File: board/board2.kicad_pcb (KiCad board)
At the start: 2 copper layers, 88 x 64 mm, 72 parts, among them J1 Battery, J2 Conn_01x06_Male, J3 Conn_ARM_JTAG_SWD_10, J4 Range_Front, J5 Range_Left, J6 Range_Right, J7 Battery, J8 Conn_02x06_Odd_Even, SW1 RST, SW2 SW_Push, SW3 SW_Push, SW4 SW_Push, U1 MIC5205-3.3YM5, U2 STM32F405RGTx, U3 DRV8848, U4 Left_Motor, U5 Right_Motor, Y1 DNP

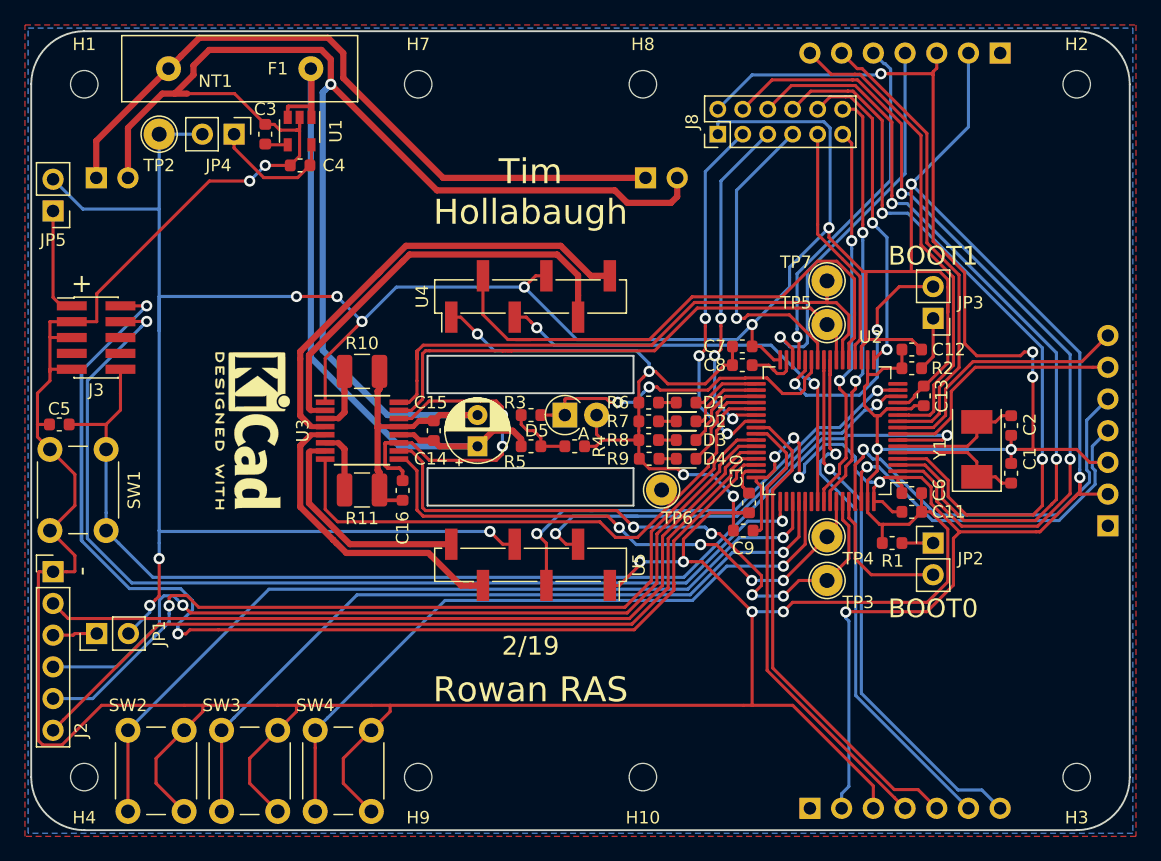
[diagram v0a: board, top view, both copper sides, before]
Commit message: Board redesign
 - add IMU6500
 - only one battery
 - half the size
 - op amp buffer on battery monitor
 - 4 layer board
 - and more
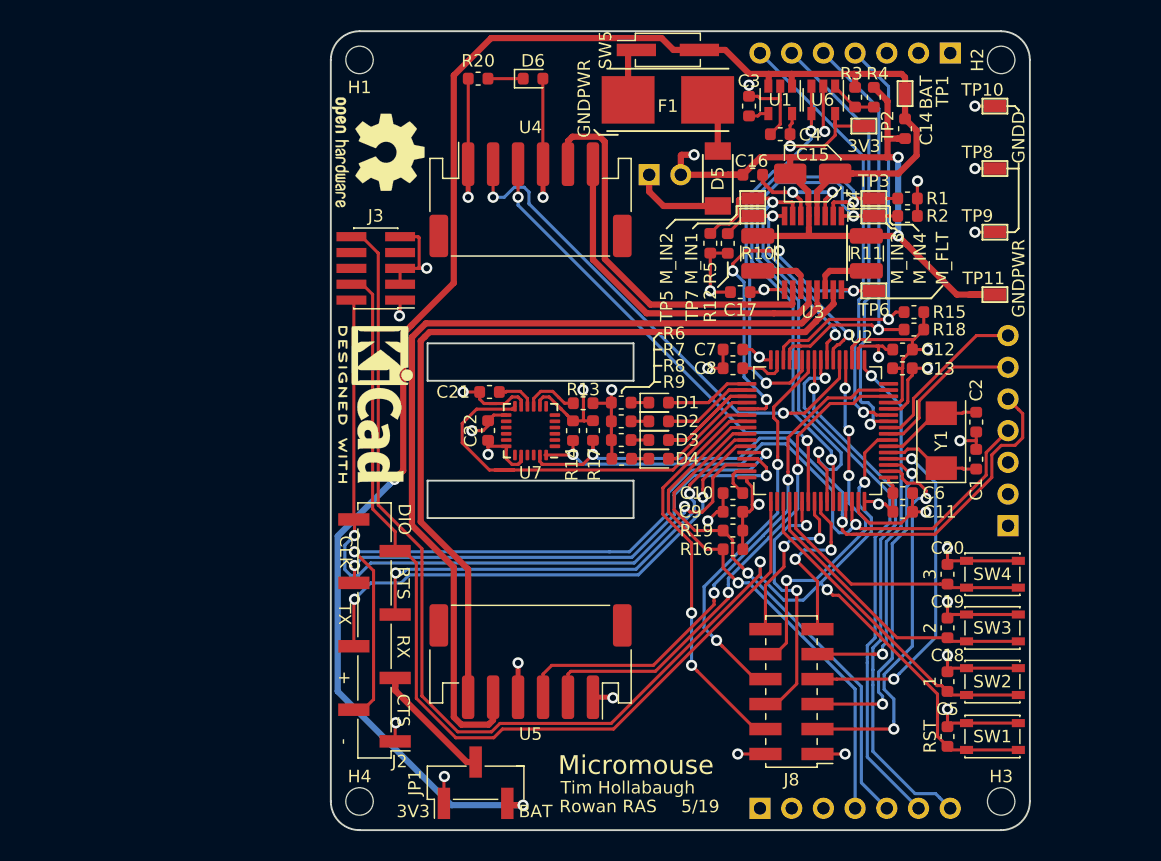
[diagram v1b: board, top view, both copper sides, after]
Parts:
- removed H10, H7, H8, H9: MountingHole, MountingHole:MountingHole_2.2mm_M2
- removed J7: Battery, Connector_PinHeader_2.54mm:PinHeader_1x02_P2.54mm_Horizontal
- removed JP2: BOOT0, Connector_PinHeader_2.54mm:PinHeader_1x02_P2.54mm_Vertical
- removed JP3: BOOT1, Connector_PinHeader_2.54mm:PinHeader_1x02_P2.54mm_Vertical
- removed JP4: BAT_PWR, Connector_PinHeader_2.54mm:PinHeader_1x02_P2.54mm_Vertical
- removed JP5: PROG_PWR, Connector_PinHeader_2.54mm:PinHeader_1x02_P2.54mm_Vertical
- added C17: 0.1uF, Capacitor_SMD:C_0603_1608Metric, F.Cu at (116.8, 88.9)
- added C18: 0.1uF, Capacitor_SMD:C_0603_1608Metric, F.Cu at (133.4, 120.1)
- added C19: 0.1uF, Capacitor_SMD:C_0603_1608Metric, F.Cu at (133.4, 115.8)
- added C20: 0.1uF, Capacitor_SMD:C_0603_1608Metric, F.Cu at (133.4, 111.5)
- added C21: 0.1uF, Capacitor_SMD:C_0603_1608Metric, F.Cu at (96.7, 96.9)
- added C22: 0.1uF, Capacitor_SMD:C_0603_1608Metric, F.Cu at (96.6, 100.0)
- added D6: WHITE, LED_SMD:LED_0603_1608Metric, F.Cu at (100.2, 71.8)
- added R12: 10k, Resistor_SMD:R_0603_1608Metric, F.Cu at (115.8, 85.0)
- added R13: 10k, Resistor_SMD:R_0603_1608Metric, F.Cu at (104.2, 97.8)
- added R14: 2.2K, Resistor_SMD:R_0603_1608Metric, F.Cu at (103.4, 100.0)
- added R15: 2.2K, Resistor_SMD:R_0603_1608Metric, F.Cu at (130.7, 90.5)
- added R16: 2.2K, Resistor_SMD:R_0603_1608Metric, F.Cu at (116.2, 109.5)
- added R17: 2.2K, Resistor_SMD:R_0603_1608Metric, F.Cu at (105.0, 100.0)
- added R18: 2.2K, Resistor_SMD:R_0603_1608Metric, F.Cu at (130.7, 91.9)
- added R19: 2.2K, Resistor_SMD:R_0603_1608Metric, F.Cu at (116.2, 108.0)
- added R20: 330, Resistor_SMD:R_0603_1608Metric, F.Cu at (95.8, 71.8)
- added REF**: OSHW-Logo2_9.8x8mm_SilkScreen, Symbol:OSHW-Logo2_9.8x8mm_SilkScreen, F.Cu at (87.8, 77.7)
- added SW5: Power, Connector_PinHeader_2.54mm:PinHeader_2x01_P2.54mm_Vertical_SMD, F.Cu at (111.0, 69.5)
- added TP1: BAT, micromouse_custom:TestPoint_Pad_1.8x1.0mm, F.Cu at (130.0, 73.0)
- added TP10: GND, micromouse_custom:TestPoint_Pad_1.8x1.0mm, F.Cu at (137.2, 74.0)
- added TP11: GND, micromouse_custom:TestPoint_Pad_1.8x1.0mm, F.Cu at (137.2, 89.1)
- added TP8: GND, micromouse_custom:TestPoint_Pad_1.8x1.0mm, F.Cu at (137.2, 79.0)
- added TP9: GND, micromouse_custom:TestPoint_Pad_1.8x1.0mm, F.Cu at (137.2, 84.1)
- added U6: MCP6001U, Package_TO_SOT_SMD:SOT-23-5, F.Cu at (123.5, 73.5)
- added U7: MPU-6500, Sensor_Motion:InvenSense_QFN-24_4x4mm_P0.5mm, F.Cu at (100.0, 100.0)
- C15: footprint Capacitor_THT:CP_Radial_D5.0mm_P2.50mm -> Capacitor_SMD:CP_Elec_4x4.5
- D1: value LED -> RED
- D2: value LED -> GREEN
- D3: value LED -> BLUE
- D4: value LED -> ORANGE
- D5: value D_Zener -> DB2441700L; footprint Diode_THT:D_T-1_P2.54mm_Vertical_AnodeUp -> micromouse_custom:SC-110A-2
- F1: value 2A -> 1A; footprint Fuse:Fuse_Littelfuse-LVR100 -> micromouse_custom:Littlefuse_154
- H1, H2, H3, H4: value MountingHole -> Corner
- J2: value Conn_01x06_Male -> Serial; footprint Connector_PinHeader_2.54mm:PinHeader_1x06_P2.54mm_Vertical -> Connector_PinHeader_2.54mm:PinHeader_1x08_P2.54mm_Vertical_SMD_Pin1Left
- J3: value Conn_ARM_JTAG_SWD_10 -> SWD
- J8: value Conn_02x06_Odd_Even -> Exp; footprint Connector_PinHeader_2.00mm:PinHeader_2x06_P2.00mm_Vertical -> Connector_PinHeader_2.00mm:PinHeader_2x06_P2.00mm_Vertical_SMD
- JP1: footprint Connector_PinHeader_2.54mm:PinHeader_1x02_P2.54mm_Vertical -> Connector_PinHeader_2.54mm:PinHeader_1x03_P2.54mm_Vertical_SMD_Pin1Left
- NT1: value Net-Tie_2 -> GND-Tie
- R1, R2: value 10K -> 10k
- R3: value 2k -> 200k
- R4: value 1k -> 100k
- R5: value 1k -> 10k
- SW1: footprint Button_Switch_THT:SW_PUSH_6mm -> Button_Switch_SMD:SW_SPST_PTS810
- SW2: value SW_Push -> Left; footprint Button_Switch_THT:SW_PUSH_6mm -> Button_Switch_SMD:SW_SPST_PTS810
- SW3: value SW_Push -> Right; footprint Button_Switch_THT:SW_PUSH_6mm -> Button_Switch_SMD:SW_SPST_PTS810
- SW4: value SW_Push -> Center; footprint Button_Switch_THT:SW_PUSH_6mm -> Button_Switch_SMD:SW_SPST_PTS810
- TP2, TP3, TP4, TP5, TP6, TP7: footprint TestPoint:TestPoint_THTPad_D2.5mm_Drill1.2mm -> micromouse_custom:TestPoint_Pad_1.8x1.0mm
- U4: footprint Connector_PinHeader_2.54mm:PinHeader_1x06_P2.54mm_Vertical_SMD_Pin1Left -> Connector_JST:JST_PH_S6B-PH-SM4-TB_1x06-1MP_P2.00mm_Horizontal
- U5: footprint Connector_PinHeader_2.54mm:PinHeader_1x06_P2.54mm_Vertical_SMD_Pin1Right -> Connector_JST:JST_PH_S6B-PH-SM4-TB_1x06-1MP_P2.00mm_Horizontal
- moved SW1 77.3 mm to (137.0, 124.5), turned to 0 degrees
- moved C5 75.4 mm to (133.4, 124.5), turned to 90 degrees
- moved SW2 70.0 mm to (137.0, 120.1), turned to 180 degrees
- moved SW3 63.5 mm to (137.0, 115.8), turned to 180 degrees
- moved SW4 57.5 mm to (137.0, 111.5), turned to 180 degrees
- moved TP2 56.5 mm to (126.7, 75.6)
- moved J8 45.0 mm to (120.9, 120.9), turned to 180 degrees
- moved C14 44.8 mm to (130.0, 75.8), turned to 270 degrees
- moved R11 44.6 mm to (126.9, 85.8), turned to 270 degrees
- moved J1 44.3 mm to (109.5, 79.5)
- moved NT1 40.9 mm to (112.6, 77.9)
- moved U3 38.8 mm to (122.6, 85.8), turned to 90 degrees
- moved C3 38.8 mm to (117.5, 74.0)
- moved U1 38.6 mm to (120.0, 73.5)
- moved C4 38.5 mm to (120.0, 76.2)
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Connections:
- C4 pad 1: Net-(C4-Pad1) -> +3V3
- D5 pad 1: /VBAT -> Net-(D5-Pad1)
- D5 pad 2: GNDD -> Net-(D5-Pad2)
- F1 pad 1: +BATT -> Net-(F1-Pad1)
- F1 pad 2: /BAT_IN -> Net-(D5-Pad1)
- J1 pad 1: /BAT_IN -> Net-(D5-Pad2)
- J3 pad 1: Net-(J3-Pad1) -> +3V3
- J3 pad 6: Net-(J3-Pad6) -> (no net)
- J3 pad 7: Net-(J3-Pad7) -> (no net)
- J3 pad 8: Net-(J3-Pad8) -> (no net)
- J4 pad 1: Net-(J4-Pad1) -> (no net)
- J5 pad 1: Net-(J5-Pad1) -> (no net)
- J6 pad 1: Net-(J6-Pad1) -> (no net)
- J6 pad 4: /R_SCL -> /R_SDA
- J6 pad 5: /R_SDA -> /R_SCL
- J8 pad 1: +3V3 -> GNDD
- J8 pad 10: /PA3 -> /PA4
- J8 pad 11: /PB4 -> /PB5
- J8 pad 12: /PB5 -> /PB4
- J8 pad 2: GNDD -> +3V3
- J8 pad 3: /PC8 -> /PC13
- J8 pad 4: /PC13 -> /PC8
- J8 pad 5: /PC7 -> /PC14
- J8 pad 6: /PC14 -> /PD2
- J8 pad 7: /PB0 -> /PC15
- J8 pad 8: /PC15 -> /PB0
- J8 pad 9: /PA4 -> /PA3
- JP1 pad 1: Net-(J2-Pad3) -> +3V3
- JP1 pad 2: +3V3 -> Net-(J2-Pad3)
- R1 pad 1: Net-(JP2-Pad1) -> /M_IN4
- R2 pad 1: Net-(JP3-Pad1) -> /M_IN3
- R4 pad 2: GNDD -> GNDPWR
- R5 pad 1: /VBAT -> /M_IN2
- R5 pad 2: Net-(R3-Pad2) -> GNDD
- U1 pad 5: Net-(C4-Pad1) -> +3V3
- U2 pad 16: /PA2 -> (no net)
- U2 pad 28: /BOOT1 -> (no net)
- U2 pad 38: /PC7 -> /IMU_INT
- U2 pad 50: /PA15 -> (no net)
- U2 pad 60: /BOOT0 -> (no net)
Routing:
- net GNDD: track 406.7 -> 125.3 mm, vias 15 -> 26
- net +3V3: track 355.3 -> 78.5 mm, vias 16 -> 13
- net +BATT: track 58.5 -> 132.7 mm, vias 0 -> 2
- net /BAT_IN: track 56.2 -> 0.00 mm
- net GNDPWR: track 116.0 -> 64.5 mm, vias 1 -> 2
- net /RM_2: track 24.5 -> 72.1 mm
- net /RM_1: track 18.2 -> 65.6 mm
- net /SWDIO: track 105.6 -> 60.0 mm
- net /BTN1: track 68.6 -> 26.7 mm, vias 1 -> 0
- net /BTN2: track 62.0 -> 24.3 mm, vias 1 -> 0
- net /PC14: track 64.4 -> 27.1 mm
- net /PC13: track 68.2 -> 31.2 mm
- net /IMU_INT: track 0.00 -> 34.0 mm
- net /BTN3: track 55.3 -> 21.5 mm, vias 1 -> 0
- net /PC15: track 60.6 -> 27.8 mm
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- added copper zone on In2.Cu, net +3V3
- added copper zone on In1.Cu, net GNDD
- removed copper zone on B.Cu, net +3V3
- removed copper zone on F.Cu, net GNDD
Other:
- board size 88 x 64 mm -> 56 x 64 mm
- copper layers 2 -> 4
- board text added: "1"
- board text added: "2"
- board text added: "3"
- board text added: "3V3"
- board text added: "5/19"
- board text added: "BAT"
- board text added: "CLK"
- board text added: "CTS"
- board text added: "DIO"
- board text added: "GNDD"
- board text added: "GNDPWR"
- board text added: "M_FLT"
- board text added: "M_IN1"
- board text added: "M_IN2"
- board text added: "M_IN3"
- board text added: "M_IN4"
- board text added: "Micromouse"
- board text added: "RST"
- board text added: "RTS"
- board text added: "RX"
- board text added: "TX"
- board text added: "Tim Hollabaugh"
- board text removed: "2/19"
- board text removed: "BOOT0"
- board text removed: "BOOT1"
- board text removed: "Battery 2"
- board text removed: "Hollabaugh"
- board text removed: "Tim"

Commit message: Final board layout
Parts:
- removed JP1: UART_PWR, Connector_PinHeader_2.54mm:PinHeader_1x03_P2.54mm_Vertical_SMD_Pin1Left
- added J7: POWER, Connector_PinHeader_2.54mm:PinHeader_1x04_P2.54mm_Vertical_SMD_Pin1Left, F.Cu at (96.8, 128.3)
- J8: value Exp -> EXP; footprint Connector_PinHeader_2.00mm:PinHeader_2x06_P2.00mm_Vertical_SMD -> Connector_PinHeader_2.00mm:PinHeader_2x07_P2.00mm_Vertical_SMD
- U4, U5: footprint Connector_JST:JST_PH_S6B-PH-SM4-TB_1x06-1MP_P2.00mm_Horizontal -> Connector_Molex:Molex_PicoBlade_53261-0671_1x06-1MP_P1.25mm_Horizontal
- moved D6 3.19 mm to (102.4, 69.5)
- moved R20 2.91 mm to (97.6, 69.5)
- moved C14 1.51 mm to (129.2, 77.1), turned to 180 degrees
- moved C21 0.90 mm to (95.8, 96.9)
- moved J8 0.90 mm to (120.9, 120.0)
- moved NT1 0.90 mm to (112.0, 77.2), turned to 90 degrees
- moved C16 0.86 mm to (118.4, 78.9), turned to 270 degrees
- moved C3 0.10 mm to (117.4, 74.0), turned to 270 degrees
- turned J3 to 0 degrees
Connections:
- J8 pad 10: /PA4 -> /PB0
- J8 pad 11: /PB5 -> /PA3
- J8 pad 12: /PB4 -> /PA4
- J8 pad 3: /PC13 -> /R_SCL
- J8 pad 4: /PC8 -> /R_SDA
- J8 pad 5: /PC14 -> /PC15
- J8 pad 6: /PD2 -> /PC8
- J8 pad 7: /PC15 -> /PC13
- J8 pad 8: /PB0 -> /PD2
- J8 pad 9: /PA3 -> /PC14
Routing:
- net /R_SDA: track 41.3 -> 63.7 mm
- net GNDPWR: track 64.5 -> 54.1 mm, vias 2 -> 0
- net +3V3: track 78.5 -> 68.6 mm, vias 13 -> 14
- net /R_SCL: track 41.4 -> 51.2 mm
- net +BATT: track 132.7 -> 123.3 mm
- net GNDD: track 125.3 -> 116.3 mm, vias 26 -> 29
- net /SWDIO: track 60.0 -> 66.8 mm
- net /~RST: track 119.9 -> 114.3 mm
- net /LED3: track 15.8 -> 10.4 mm
- net /LED1: track 11.4 -> 6.90 mm
- net /PC14: track 27.1 -> 22.9 mm
- net /PC15: track 27.8 -> 31.3 mm
- net /PC13: track 31.2 -> 27.8 mm
- net /PD2: track 22.3 -> 19.3 mm
- net /PA4: track 30.4 -> 27.5 mm
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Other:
- rule pad_to_mask_clearance: 0.051 -> 0.05
- rule solder_mask_min_width: 0.25 -> 0.05
- board text added: "GND"
- board text added: "SER"

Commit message: board: fix imu footprint
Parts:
- U7: footprint Sensor_Motion:InvenSense_QFN-24_4x4mm_P0.5mm -> Sensor_Motion:InvenSense_QFN-24_3x3mm_P0.4mm
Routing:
- net GNDD: track 116.3 -> 117.1 mm
- net +3V3: track 68.6 -> 69.1 mm
- net /F_SCL: track 56.5 -> 57.1 mm
